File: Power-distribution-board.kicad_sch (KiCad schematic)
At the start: 79 parts, among them J1 178.6165.0001 breaker, J10 2606-1104/020-000, J12 2606-1104/020-000, J13 2606-1104/020-000, J15 2606-1104/020-000, J16 2606-1104/020-000, J2 178.6165.0001 breaker, J3 178.6165.0001 breaker, J4 178.6165.0001 breaker, J5 178.6165.0001 breaker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

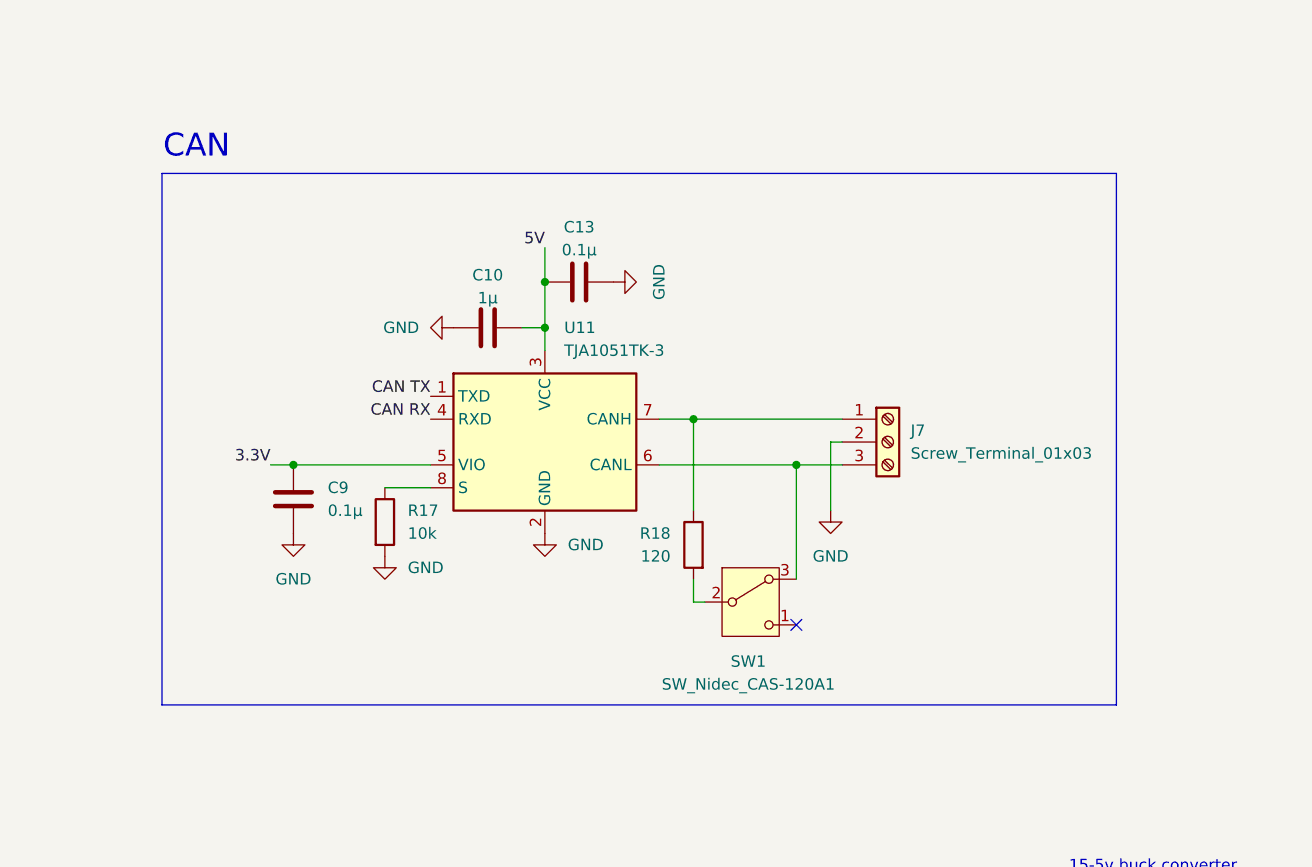
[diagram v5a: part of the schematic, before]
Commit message: update layout
added board edge and planes
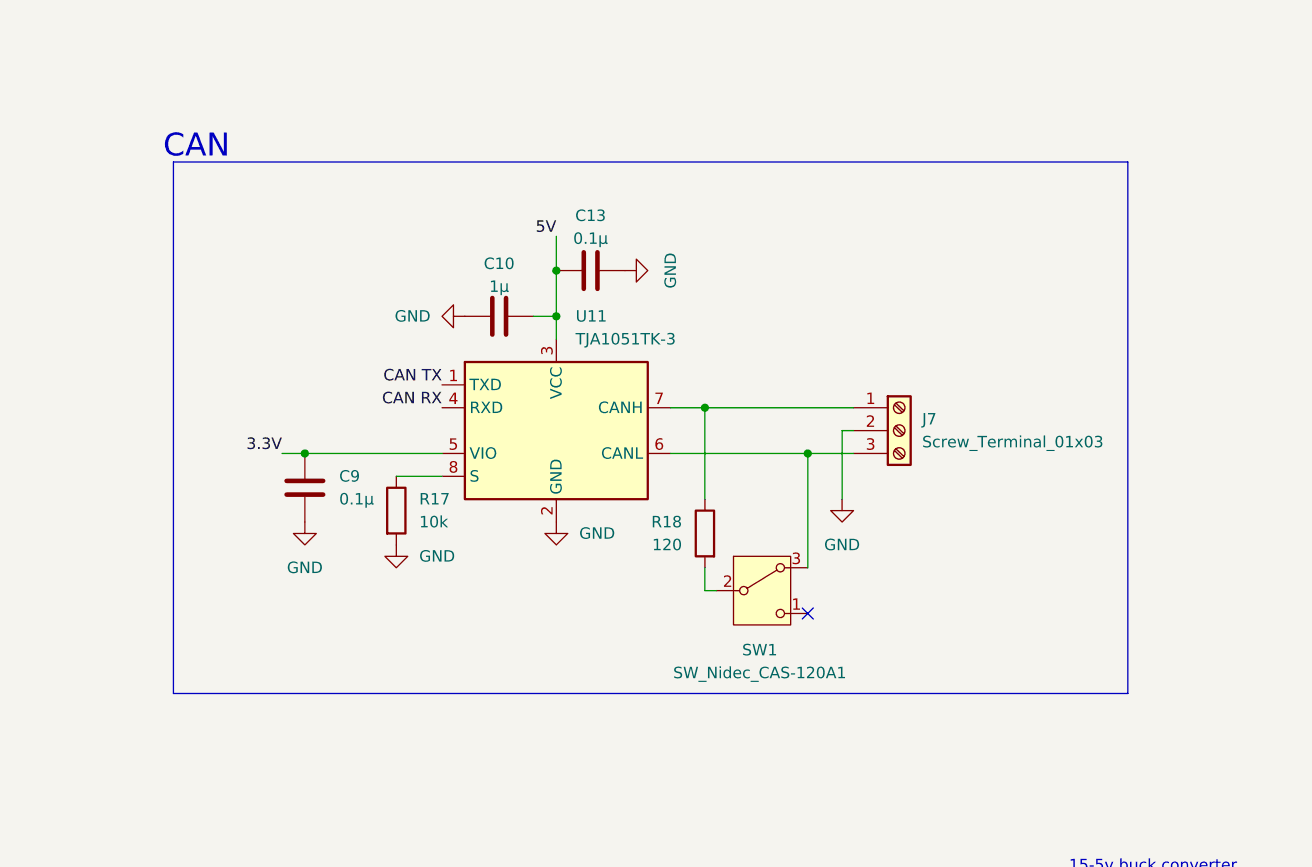
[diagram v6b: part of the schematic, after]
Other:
- moved on the sheet: C10, C13, C9, J7, R17, R18, SW1, U11

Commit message: added 4-digit display & pwr planes
add 4digit led and tm1637 driver
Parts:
- added C25, C29: 0.1u, Capacitor_SMD:C_0201_0603Metric, symbol Device:C
- added C26: 10u, Capacitor_SMD:C_0402_1005Metric, symbol Device:C
- added C27, C28: 100p, Capacitor_SMD:C_0402_1005Metric, symbol Device:C
- added C30: 100u, Capacitor_SMD:CP_Elec_3x5.4, symbol Device:C_Polarized
- added R3, R4: 10k, Resistor_SMD:R_0402_1005Metric, symbol Device:R
- added U5: TM1637, pdb_footprints:LED_driver_TM1637, symbol PDB_symbols:TM1637
- added U6: CC56-12EWA, Display_7Segment:CA56-12EWA, symbol Display_Character:CC56-12EWA
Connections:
- net 3.3V: now also C25.2
- net 5V: now also C29.2, C30.1, R3.1, R4.1, U5.16 (VDD)
- net GND: now also C26.1, C27.1, C28.2, C29.1, C30.2, U5.1 (GND)
- net CLK: now reaches U1.31 (IO38)
- net CLK: now also C27.2, R3.2, U5.18 (CLK)
- net DIO: now reaches U1.32 (IO39)
- net DIO: now also C28.1, R4.2, U5.17 (DIO)
- new net: U5.6 (SEG5/KS5), U6.1 (e)
- new net: U5.7 (SEG6/KS6), U6.10 (f)
- new net: U5.2 (SEG1/KS1), U6.11 (a)
- new net: U5.15 (GRID1), U6.12 (CC1)
- new net: U5.5 (SEG4/KS4), U6.2 (d)
- new net: U5.9 (SEG8/KS8), U6.3 (DPX)
- new net: U5.4 (SEG3/KS3), U6.4 (c)
- new net: U5.8 (SEG7/KS7), U6.5 (g)
- new net: U5.12 (GRID4), U6.6 (CC4)
- new net: U5.3 (SEG2/KS2), U6.7 (b)
- new net: U5.13 (GRID3), U6.8 (CC3)
- new net: U5.14 (GRID2), U6.9 (CC2)
- new net: C25.1, C26.2
- no-connect marks 62 -> 64
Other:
- note added: "4-digit 7-segment LED display"
- moved on the sheet: C10, C13, C2, C22, C23, C3, C32, C4, C5, C6, C7, C8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
